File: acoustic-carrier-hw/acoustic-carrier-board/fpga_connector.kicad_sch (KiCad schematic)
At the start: 1 part, among them IC1 ECP5-BGA256

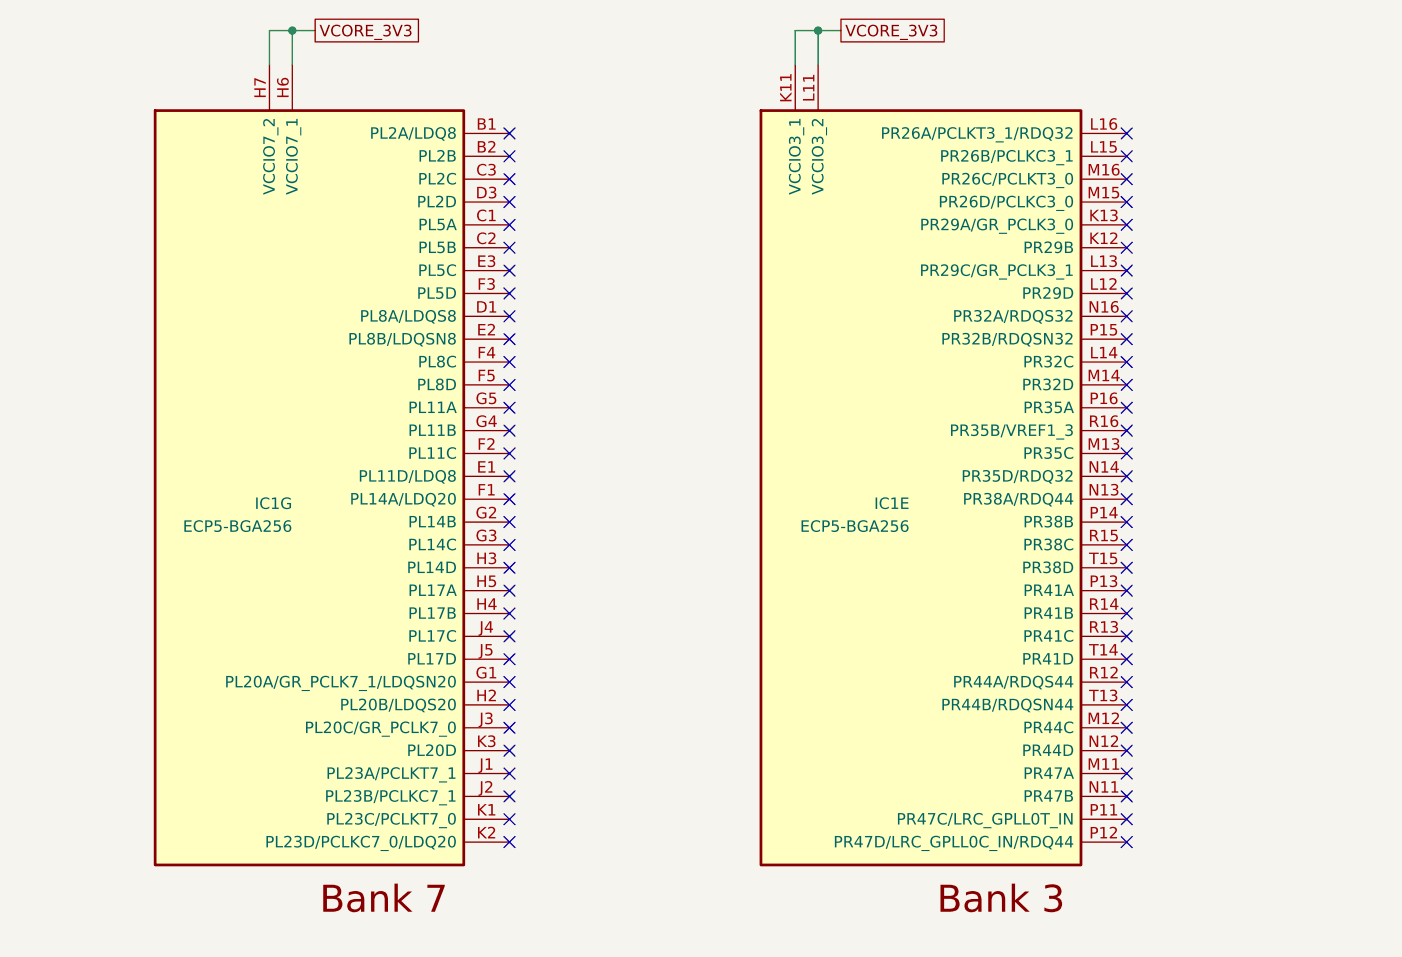
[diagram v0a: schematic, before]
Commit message: [carrier] Added 100 MHz crystal oscillator (next) Do a component / footprint check
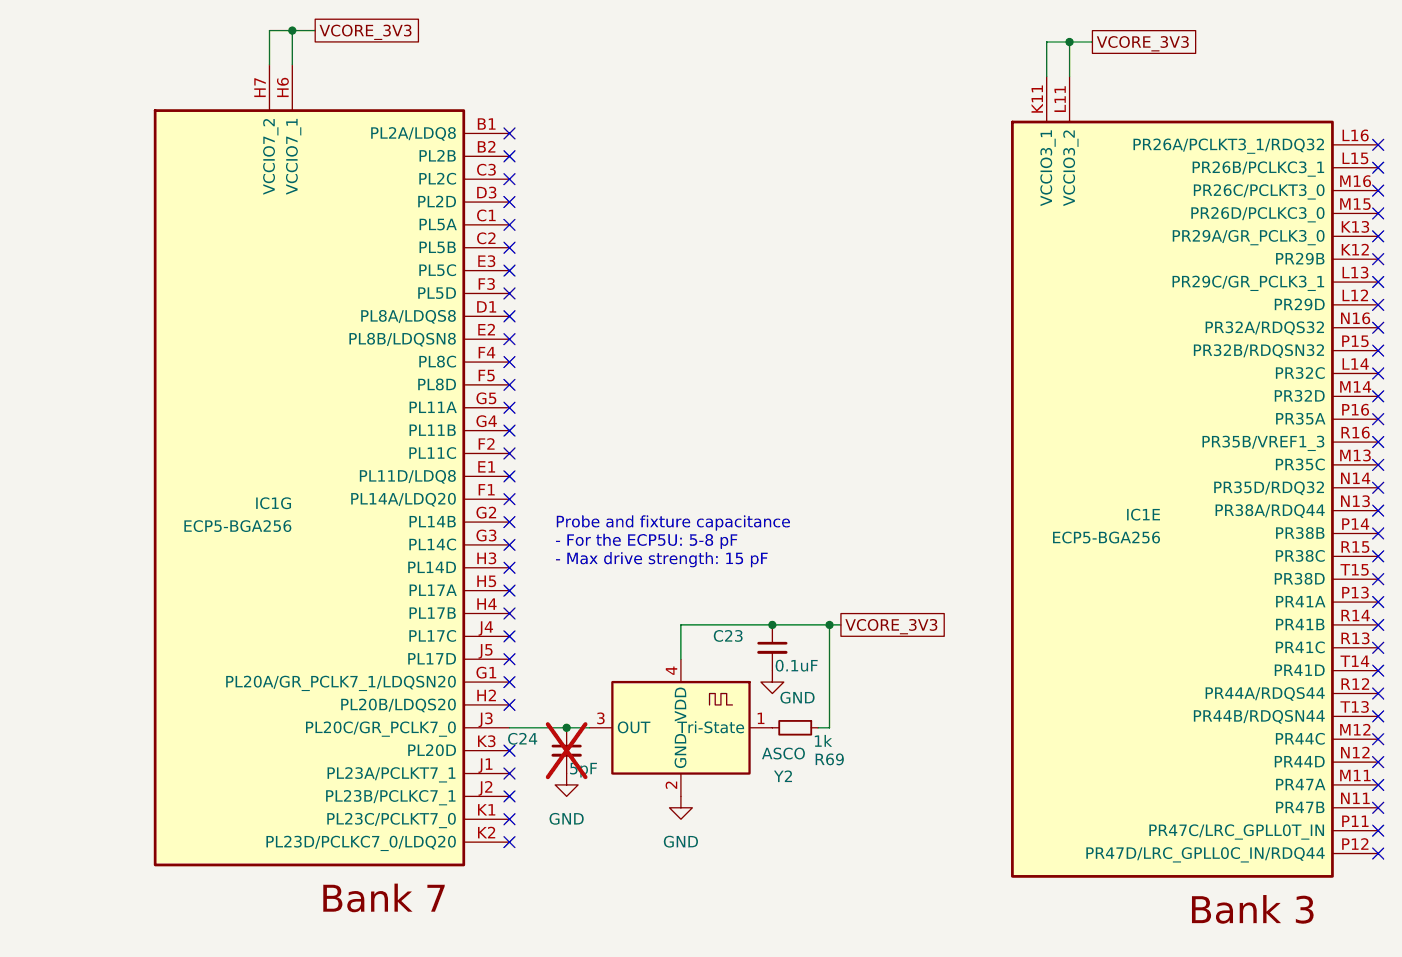
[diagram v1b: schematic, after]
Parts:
- added C23: 0.1uF, Capacitor_SMD:C_0402_1005Metric, symbol Device:C_Small
- added C24: 5pF, Capacitor_SMD:C_0603_1608Metric, symbol Device:C_Small
- added R69: 1k, Resistor_SMD:R_0603_1608Metric, symbol Device:R_Small
- added Y2: ASCO, Crystal:Crystal_SMD_3225-4Pin_3.2x2.5mm, symbol Oscillator:ASCO
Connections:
- net VCORE_3V3: now also C23.1, R69.1, Y2.4 (VDD)
- net at IC1.J3 (PL20C/GR_PCLK7_0): now also C24.1, Y2.3 (OUT)
- new net: R69.2, Y2.1 (Tri-State)
- new net GND: C23.2, C24.2, Y2.2 (GND)
- no-connect marks 64 -> 63
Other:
- note added: "Probe and fixture capacitance - For the ECP5U: 5-8 pF - Max drive strength: 15 pF"
- moved on the sheet: IC1E

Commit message: [carrier] Reorganized schematic, moPut adc signals in bus, fixed DRC errors (next) recheck ethernet, check usb, add power switch
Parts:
- removed unit 5 of IC1
- Y2: value ASCO -> Crystal Oscillator
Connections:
- no-connect marks 63 -> 31

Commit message: [carrier] Fixed error in ethernet power supply, separated footprints + symbols into library (next) check whether supply should be DVDDH
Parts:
- removed IC1: ECP5-BGA256, fpga:BGA256C80P16X16_1400X1400X170, symbol ecp5bga256:ECP5-BGA256
- added IC1: ECP5-BGA256, iw-fpga_mcu:BGA256C80P16X16_1400X1400X170, symbol iw-fpga_mcu:ECP5-BGA256
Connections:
- net VCORE_3V3: now also IC1.H6 (VCCIO7_1), IC1.H7 (VCCIO7_2)
- net at C24.1, Y2.3 (OUT): now also IC1.J3 (PL20C/GR_PCLK7_0)
